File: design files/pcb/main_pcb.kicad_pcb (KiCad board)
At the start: 2 copper layers, 29 x 85 mm, 43 parts, among them J1 IN, J2 OUT, J3 INVOUT, U1 TL074CJ, U2 TL072IPE4

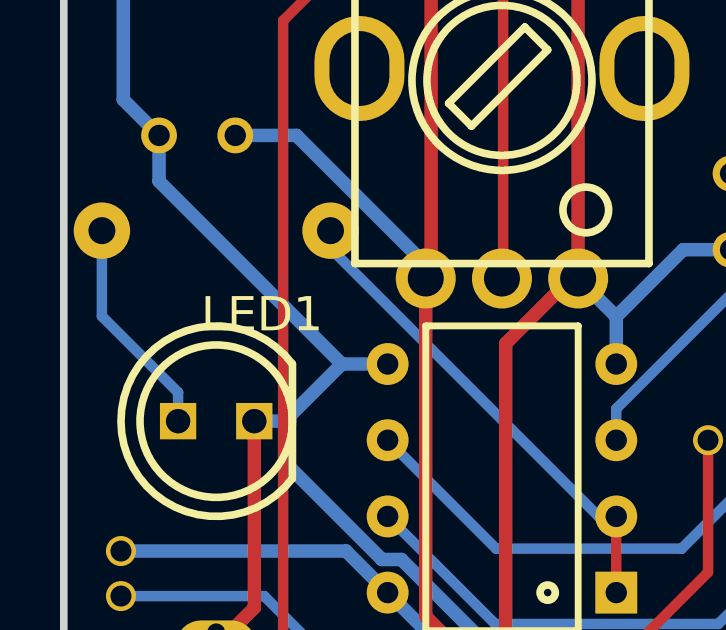
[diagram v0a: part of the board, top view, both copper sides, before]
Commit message: slight changes to pcb silkscreen
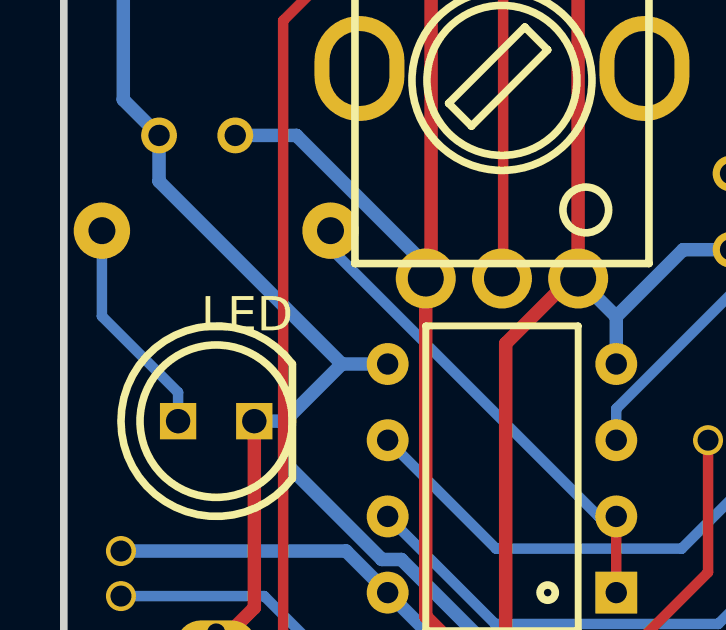
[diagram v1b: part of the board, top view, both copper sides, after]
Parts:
- removed LED1: LED_LED5MM, easyeda:LED_LED5MM
- added LED: LED_LED5MM, easyeda:LED_LED5MM, F.Cu at (10.2, 144.9)
- D1, D2: value DIODE1N4148 -> 1n4148
- D3: value DIODE1N4148 -> 1N4148

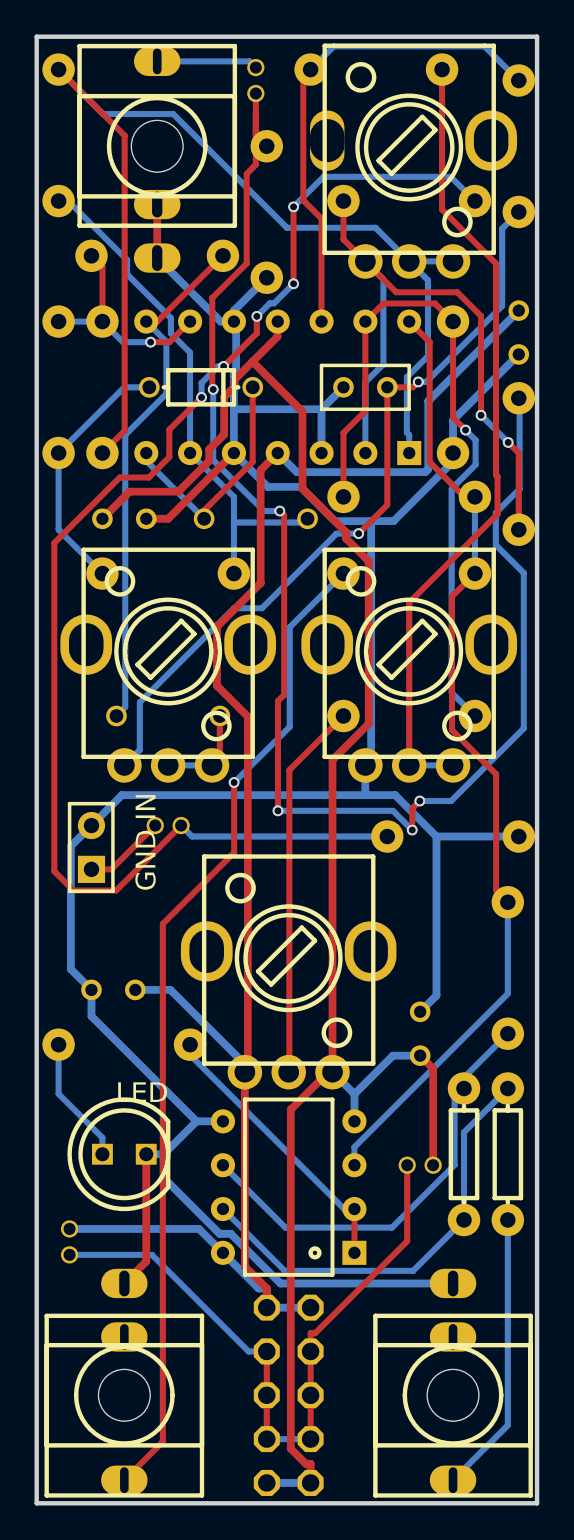
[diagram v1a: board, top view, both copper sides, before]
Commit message: Version 1.2 fixes, changed Guitar jack orientation and resistor for more amplification!
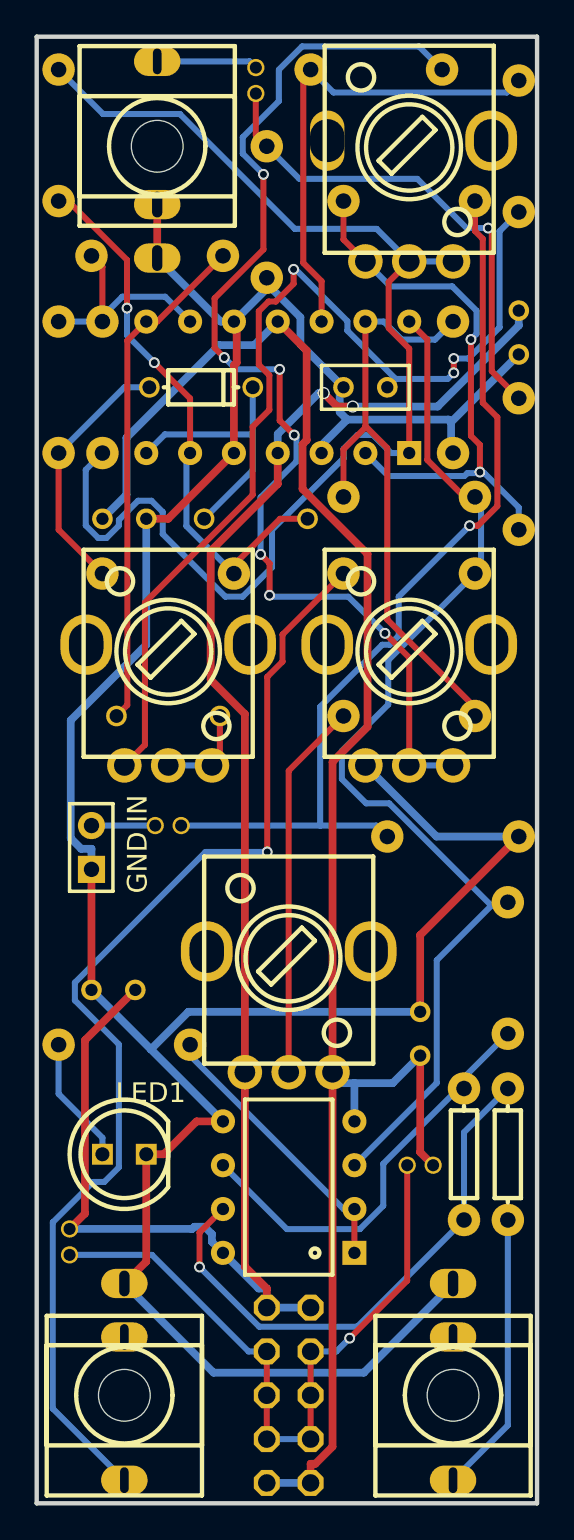
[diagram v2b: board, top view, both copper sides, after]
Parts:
- removed LED: LED_LED5MM, easyeda:LED_LED5MM
- added LED1: LED_LED5MM, easyeda:LED_LED5MM, F.Cu at (10.2, 144.9)
- D1, D2: value 1n4148 -> DIODE1N4148
- D3: value 1N4148 -> DIODE1N4148
- R10: value 10k -> 4.7k
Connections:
- C3 pad 1: H1_1 -> H1_2
- H1 pad 1: H1_1 -> GND
- H1 pad 2: GND -> H1_2
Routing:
- net C1_2: track 85.4 -> 28.7 mm, vias 5 -> 1
- net R10_2: track 79.0 -> 53.7 mm, vias 5 -> 1
- net R7_2: track 46.3 -> 66.5 mm, vias 0 -> 7
- net C2_2: track 44.4 -> 58.0 mm, vias 2 -> 3
- net U1_1: track 63.9 -> 73.3 mm
- net R12_2: track 57.8 -> 65.8 mm
- net LED: track 56.4 -> 63.0 mm
- net U2_7: track 25.3 -> 31.9 mm, vias 0 -> 1
- net 12V: track 98.1 -> 104.0 mm, vias 0 -> 2
- net U1_13: track 41.2 -> 36.0 mm, vias 1 -> 0
- net H1_1: track 4.75 -> 0.00 mm
- net U1_2: track 37.3 -> 33.0 mm
- net H1_2: track 0.00 -> 3.69 mm
- net GND: track 167.4 -> 169.7 mm
- net U1_6: track 30.5 -> 32.2 mm, vias 0 -> 2
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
